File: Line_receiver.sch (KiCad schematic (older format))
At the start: 16 parts, among them U15 LME49740, U16 LME49740

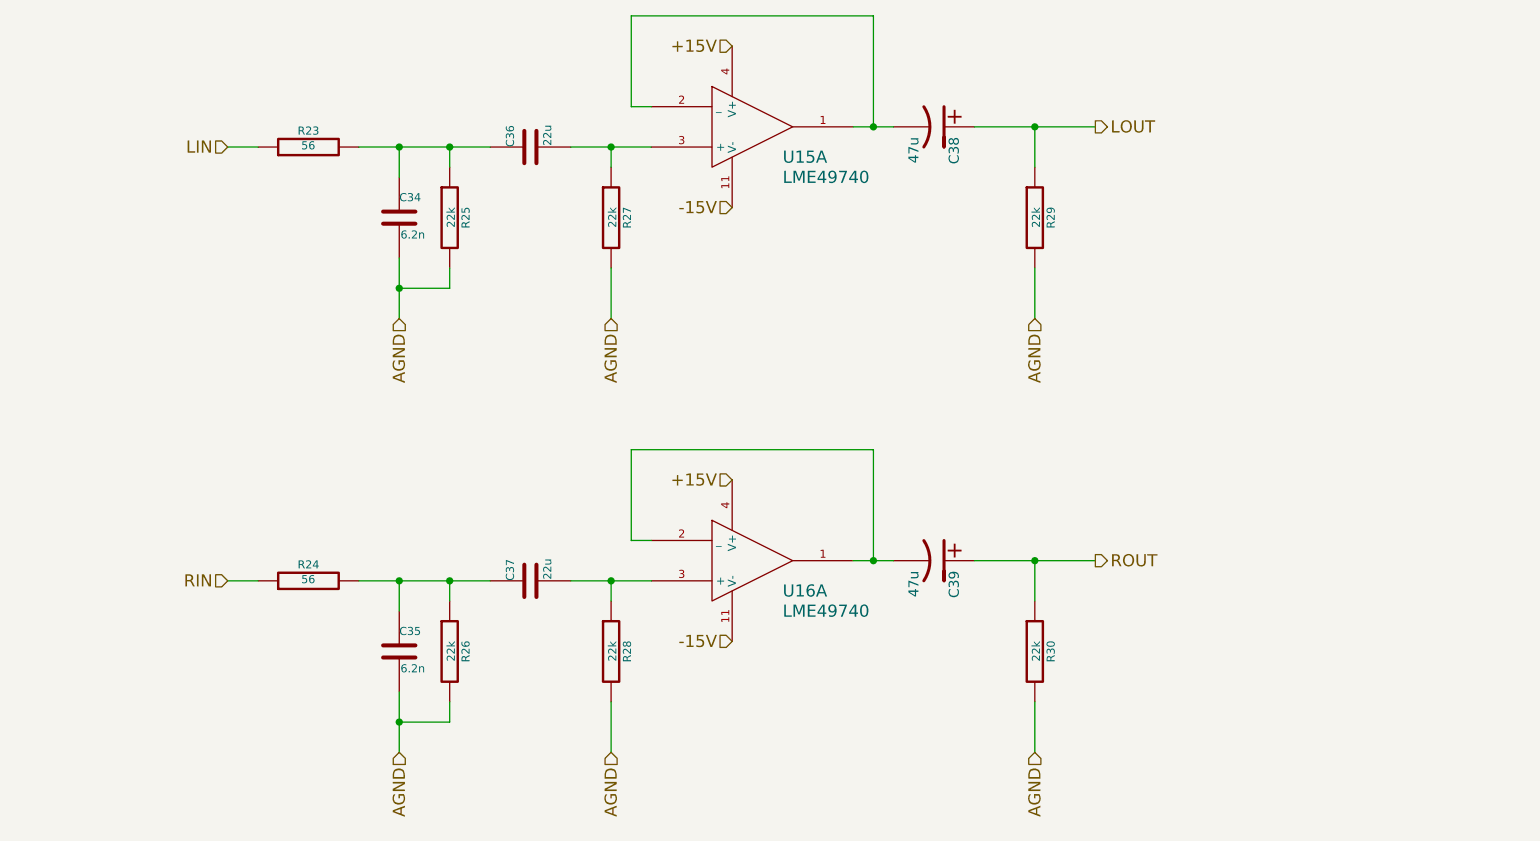
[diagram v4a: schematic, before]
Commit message: A lot of routing, some parts changes:   * Added snubber C/RC snubbers to transformer secondaries.   * Changed PSU OA from OPA209 to OPA27.   * Routed external PSU.   * Mostly done routing internal circuits.  Just need to get everything together.   * Changed digital transformer to a more appropriately-specced one.
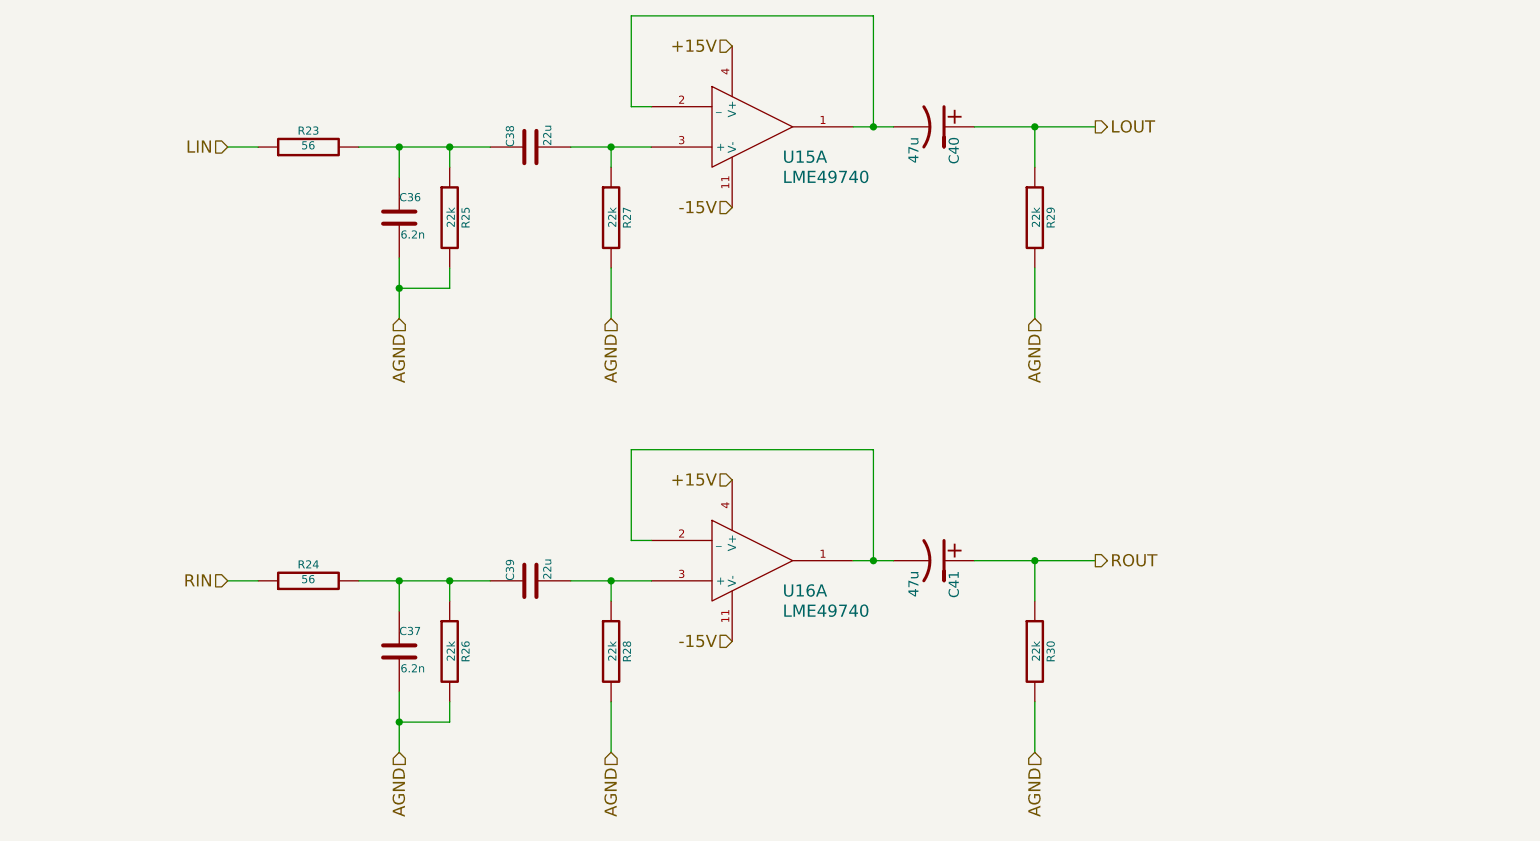
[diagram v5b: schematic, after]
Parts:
- renumbered C34 to C36, C35 to C37, C36 to C38, C37 to C39, C38 to C40, C39 to C41
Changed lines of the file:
@@
 $EndComp
 $Comp
-L C C34
+L C C36
 U 1 1 536E032E
 P 3850 3050
-F 0 "C34" H 3850 3150 40  0000 L CNN
+F 0 "C36" H 3850 3150 40  0000 L CNN
 F 1 "6.2n" H 3856 2965 40  0000 L CNN
 F 2 "Capacitors_ThroughHole:Capacitor18x7RM15" H 3888 2900 30  0001 C CNN
@@
 $EndComp
 $Comp
-L C C36
+L C C38
 U 1 1 536E032F
 P 4500 2700
-F 0 "C36" H 4500 2800 40  0000 L CNN
+F 0 "C38" H 4500 2800 40  0000 L CNN
 F 1 "22u" H 4506 2615 40  0000 L CNN
 F 2 "Capacitors_ThroughHole:Capacitor5x11RM2.5" H 4538 2550 30  0001 C CNN
@@
 -15V
 $Comp
-L CP1 C38
+L CP1 C40
 U 1 1 536E0333
 P 6500 2600
-F 0 "C38" H 6550 2700 50  0000 L CNN
+F 0 "C40" H 6550 2700 50  0000 L CNN
 F 1 "47u" H 6550 2500 50  0000 L CNN
 F 2 "Capacitors_Elko_ThroughHole:Elko_vert_DM5_RM2" H 6500 2600 60  0001 C CNN
@@
 	7300 2600 6700 2600
 $Comp
-L C C35
+L C C37
 U 1 1 536E0ADA
 P 3850 5200
-F 0 "C35" H 3850 5300 40  0000 L CNN
+F 0 "C37" H 3850 5300 40  0000 L CNN
 F 1 "6.2n" H 3856 5115 40  0000 L CNN
 F 2 "Capacitors_ThroughHole:Capacitor18x7RM15" H 3888 5050 30  0001 C CNN
@@
 $EndComp
 $Comp
-L C C37
+L C C39
 U 1 1 536E0AE0
 P 4500 4850
-F 0 "C37" H 4500 4950 40  0000 L CNN
+F 0 "C39" H 4500 4950 40  0000 L CNN
 F 1 "22u" H 4506 4765 40  0000 L CNN
 F 2 "Capacitors_ThroughHole:Capacitor5x11RM2.5" H 4538 4700 30  0001 C CNN
@@
 -15V
 $Comp
-L CP1 C39
+L CP1 C41
 U 1 1 536E0AFC
 P 6500 4750
-F 0 "C39" H 6550 4850 50  0000 L CNN
+F 0 "C41" H 6550 4850 50  0000 L CNN
 F 1 "47u" H 6550 4650 50  0000 L CNN
 F 2 "Capacitors_Elko_ThroughHole:Elko_vert_DM5_RM2" H 6500 4750 60  0001 C CNN

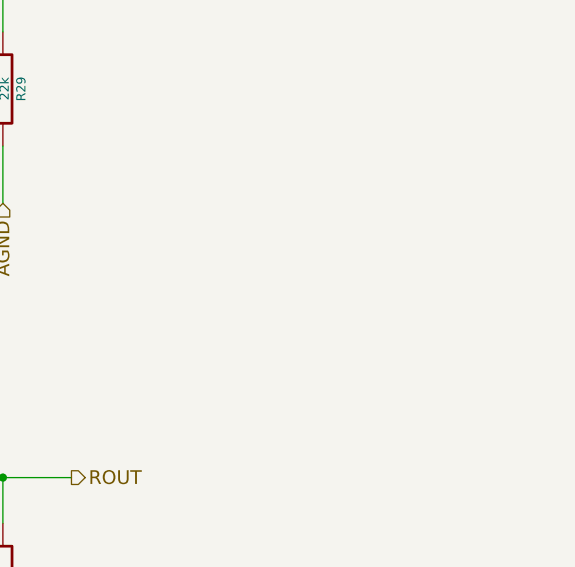
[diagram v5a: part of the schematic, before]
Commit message: First complete version.   * Added 10uF decoupling capacitors to the start of each signal processing section.   * Completed routing.  A few -18 V nets remain unrouted; these will be wired in.
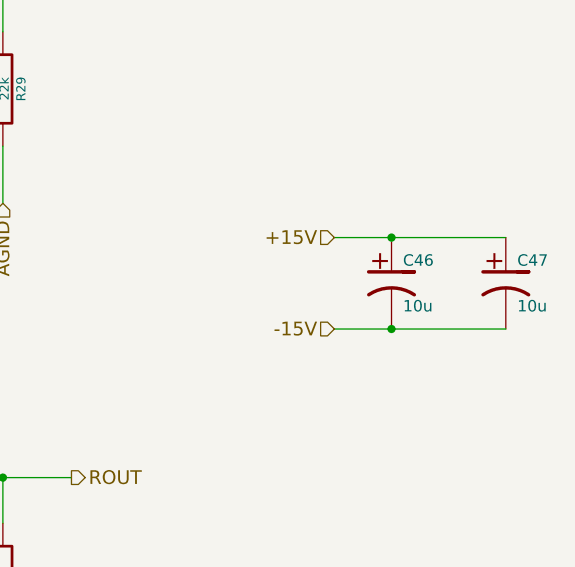
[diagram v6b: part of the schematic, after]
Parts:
- added C46, C47: 10u, Capacitors_Elko_ThroughHole:Elko_vert_DM5_RM2-5, symbol CP1
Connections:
- net +15V: now also C46.1, C47.1
- net -15V: now also C46.2, C47.2
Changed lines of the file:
@@
+	1    0    0    -1
+$EndComp
+$Comp
+L CP1 C46
+U 1 1 538C7349
+P 8700 3900
+F 0 "C46" H 8750 4000 50  0000 L CNN
+F 1 "10u" H 8750 3800 50  0000 L CNN
+F 2 "Capacitors_Elko_ThroughHole:Elko_vert_DM5_RM2-5" H 8700 3900 60  0001 C CNN
+F 3 "" H 8700 3900 60  0000 C CNN
+F 4 "478-6062-ND" H 8700 3900 60  0001 C CNN "DigiKey"
+	1    8700 3900
+	1    0    0    -1
+$EndComp
+Text HLabel 8450 3700 0    60   Input ~ 0
++15V
+Text HLabel 8450 4100 0    60   Input ~ 0
+-15V
+Wire Wire Line
+	8450 3700 9200 3700
+Connection ~ 8700 3700
+Wire Wire Line
+	8450 4100 9200 4100
+Connection ~ 8700 4100
+$Comp
+L CP1 C47
+U 1 1 538C74B3
+P 9200 3900
+F 0 "C47" H 9250 4000 50  0000 L CNN
+F 1 "10u" H 9250 3800 50  0000 L CNN
+F 2 "Capacitors_Elko_ThroughHole:Elko_vert_DM5_RM2-5" H 9200 3900 60  0001 C CNN
+F 3 "" H 9200 3900 60  0000 C CNN
+F 4 "478-6062-ND" H 9200 3900 60  0001 C CNN "DigiKey"
+	1    9200 3900
 	1    0    0    -1
 $EndComp
